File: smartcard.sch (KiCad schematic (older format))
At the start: 4 parts, among them P1000 ISO7816_NO

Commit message: [cleanup] updating project files for LEIA
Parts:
- P1000: footprint wookey:VJW53666 -> leia:VJW53666; symbol wookey:ISO7816_NO -> leia:ISO7816_NO
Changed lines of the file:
@@
 EESchema Schematic File Version 4
-LIBS:wookey-cache
+LIBS:leia-cache
 EELAYER 29 0
 EELAYER END
@@
 $EndDescr
 $Comp
-L wookey:ISO7816_NO P1000
+L leia:ISO7816_NO P1000
 U 1 1 583DE412
 P 11350 8000
 F 0 "P1000" H 11350 8300 60  0000 C CNN
 F 1 "ISO7816_NO" H 11350 7350 60  0000 C CNN
-F 2 "wookey:VJW53666" H 11350 8000 30  0001 C CNN
+F 2 "leia:VJW53666" H 11350 8000 30  0001 C CNN
 F 3 "http://fr.rs-online.com/web/p/supports-de-carte-sim-et-memoire/5427911/" H 11350 8000 30  0001 C CNN
 F 4 "Amphenol FCI" H 11350 8000 60  0001 C CNN "MFG Name"
@@
 $EndComp
 $Comp
-L wookey:GND #PWR0128
+L leia:GND #PWR0128
 U 1 1 583E1B51
 P 12050 8950
@@
 Connection ~ 11950 7350
 $Comp
-L wookey:GND #PWR0129
+L leia:GND #PWR0129
 U 1 1 583F161E
 P 11950 7350
@@
 	10500 7550 10500 7350
 $Comp
-L wookey:+3V3 #PWR0130
+L leia:+3V3 #PWR0130
 U 1 1 5A023985
 P 10500 7350
@@
 CARD_IO
 $Comp
-L wookey:GND #PWR0131
+L leia:GND #PWR0131
 U 1 1 5B01D1B7
 P 10050 6400
@@
 $EndComp
 $Comp
-L wookey:+3V3 #PWR0132
+L leia:+3V3 #PWR0132
 U 1 1 5B01D334
 P 10050 6150

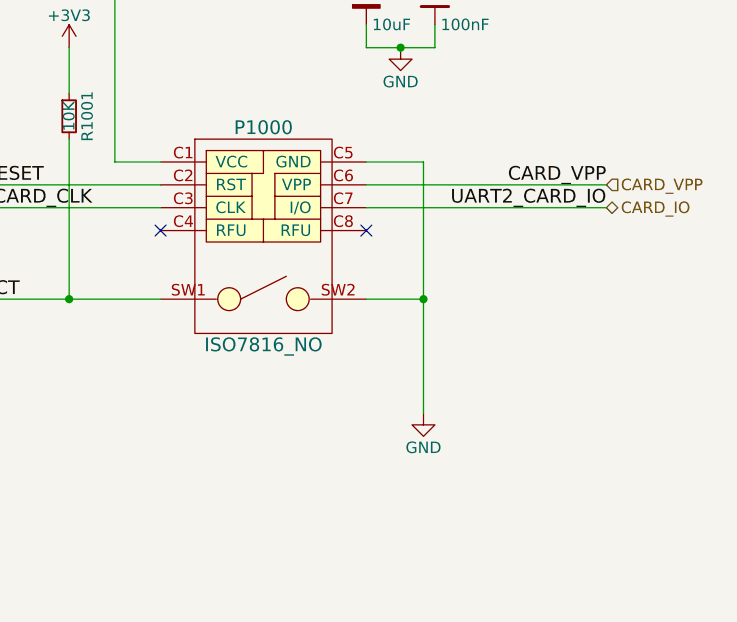
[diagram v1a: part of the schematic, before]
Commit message: [enhancement] Adding rshunt
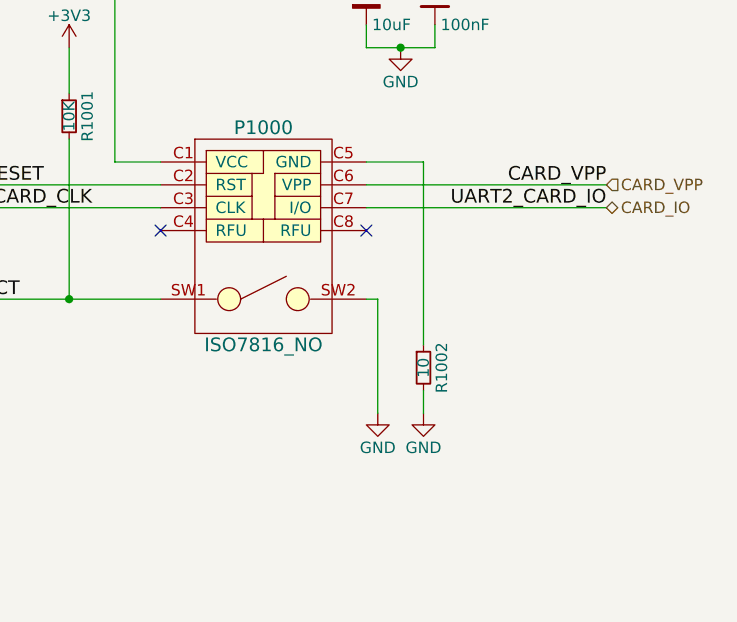
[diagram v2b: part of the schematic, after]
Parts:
- added R1002: 10, Resistor_SMD:R_0603_1608Metric, symbol Device:R_Small
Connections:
- net GND: now also R1002.2; no longer P1000.C5 (GND)
- new net: P1000.C5 (GND), R1002.1
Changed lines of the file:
@@
 $Descr A2 23386 16535
 encoding utf-8
-Sheet 5 6
-Title "Wookey Motherboard"
+Sheet 3 4
+Title "LEIA Motherboard"
 Date "2019-05-16"
 Rev ""
@@
 	11800 7850 12050 7850
 Wire Wire Line
-	12050 7850 12050 8450
-Wire Wire Line
-	11800 8450 12050 8450
-Connection ~ 12050 8450
-Wire Wire Line
 	9500 7950 10900 7950
 Wire Wire Line
@@
 Text Notes 9850 6900 0    60   ~ 0
 The smartcard is powered by U500 GPIO
-Wire Wire Line
-	12050 8450 12050 8950
 Wire Wire Line
 	10500 8450 10900 8450
@@
 Wire Wire Line
 	12100 7000 12100 7050
+$Comp
+L Device:R_Small R1002
+U 1 1 5CF7CF14
+P 12050 8750
+F 0 "R1002" V 12130 8750 50  0000 C CNN
+F 1 "10" V 12050 8750 50  0000 C CNN
+F 2 "Resistor_SMD:R_0603_1608Metric" V 11980 8750 30  0001 C CNN
+F 3 "" H 12050 8750 30  0000 C CNN
+F 4 "FARNELL" H 1550 1050 50  0001 C CNN "Distrib"
+F 5 "https://fr.farnell.com/vishay/crcw060310k0fkeahp/res-couche-epaisse-10k-1-0-25w/dp/1738918" H 1550 1050 50  0001 C CNN "Distrib Link"
+F 6 "1738918" H 1550 1050 50  0001 C CNN "Distrib PN"
+F 7 "Vishay" H 1550 1050 50  0001 C CNN "MFG Name"
+F 8 "CRCW060310K0FKEAHP" H 1550 1050 50  0001 C CNN "MFG Part Num"
+	1    12050 8750
+	1    0    0    -1
+$EndComp
+Wire Wire Line
+	12050 8850 12050 8950
+$Comp
+L leia:GND #PWR0103
+U 1 1 5CF7F199
+P 11850 8950
+F 0 "#PWR0103" H 11850 8700 50  0001 C CNN
+F 1 "GND" H 11850 8800 50  0000 C CNN
+F 2 "" H 11850 8950 60  0000 C CNN
+F 3 "" H 11850 8950 60  0000 C CNN
+	1    11850 8950
+	1    0    0    -1
+$EndComp
+Wire Wire Line
+	12050 7850 12050 8650
+Wire Wire Line
+	11850 8950 11850 8450
+Wire Wire Line
+	11850 8450 11800 8450
 $EndSCHEMATC
